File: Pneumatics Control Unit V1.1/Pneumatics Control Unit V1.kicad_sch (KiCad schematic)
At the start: 69 parts, among them J1 RX_PORT, J10 Conn_01x02_Male, J11 Conn_01x02_Male, J12 10118194-0001LF, J2 RX_PORT, J3 MICROMOD-2222, J4 Conn_01x02_Male, J5 Conn_01x02_Male, J6 Conn_01x02_Male, J7 Conn_01x02_Male, J8 Conn_01x02_Male, J9 Conn_01x02_Male, U1 ISL83490IBZ, U2 MIC2178-3.3YWM, U3 MC78M05CDTRKG

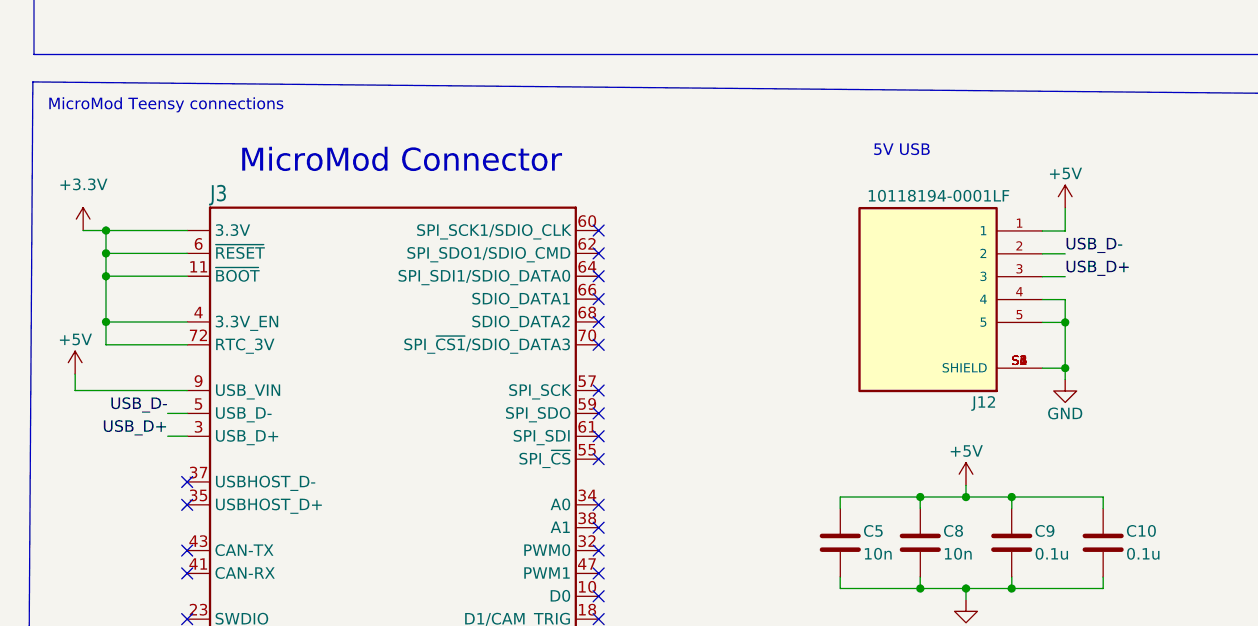
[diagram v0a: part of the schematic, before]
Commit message: Adding better m.2 connector
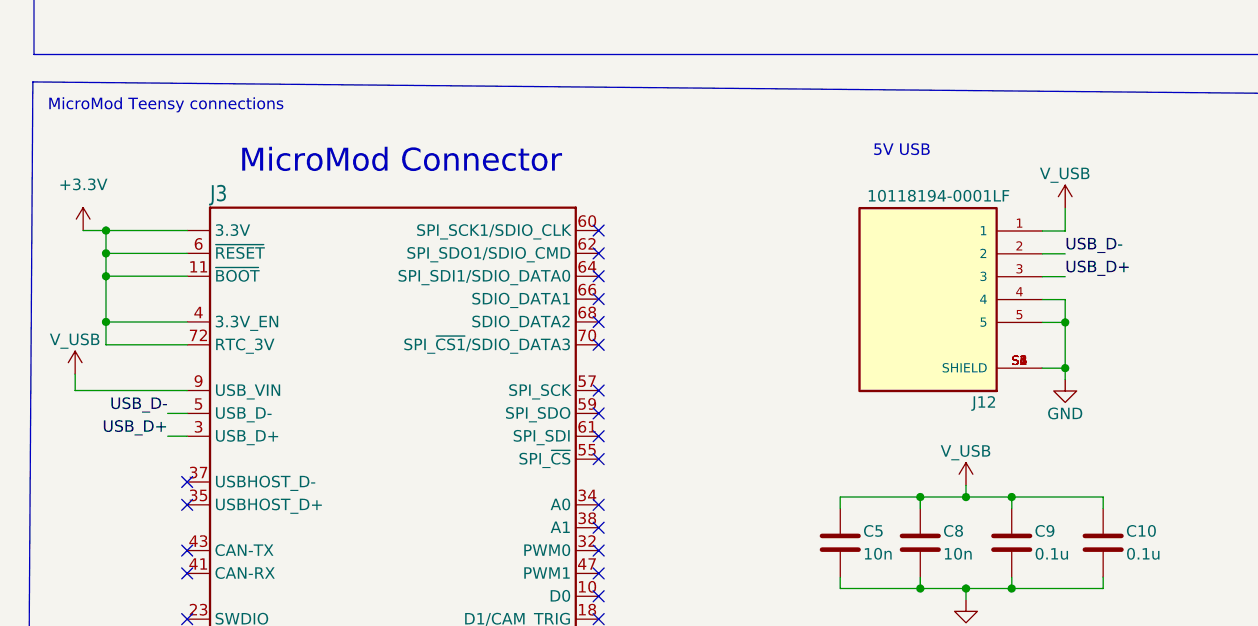
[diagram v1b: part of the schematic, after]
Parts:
- J3: footprint m2:MDT420M02001 -> mm-m:M.2-CONNECTOR-E
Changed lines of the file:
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@@
       (effects (font (size 1.27 1.27)) hide)
     )
-    (property "Value" "+5V" (id 1) (at 20.193 129.4892 0))
+    (property "Value" "V_USB" (id 1) (at 20.193 129.4892 0))
     (property "Footprint" "" (id 2) (at 20.193 133.2992 0)
       (effects (font (size 1.27 1.27)) hide)
@@
       (effects (font (size 1.778 1.5113)) (justify left bottom))
     )
-    (property "Footprint" "m2:MDT420M02001" (id 2) (at 55.499 168.148 0)
+    (property "Footprint" "mm-m:M.2-CONNECTOR-E" (id 2) (at 55.499 168.148 0)
       (effects (font (size 1.27 1.27)) hide)
     )
@@
       (effects (font (size 1.27 1.27)) hide)
     )
-    (property "Value" "+5V" (id 1) (at 130.2004 111.0488 0))
+    (property "Value" "V_USB" (id 1) (at 130.2004 111.0488 0))
     (property "Footprint" "" (id 2) (at 130.2004 114.8588 0)
       (effects (font (size 1.27 1.27)) hide)
@@
       (effects (font (size 1.27 1.27)) hide)
     )
-    (property "Value" "+5V" (id 1) (at 119.1768 141.8844 0))
+    (property "Value" "V_USB" (id 1) (at 119.1768 141.8844 0))
     (property "Footprint" "" (id 2) (at 119.1768 145.6944 0)
       (effects (font (size 1.27 1.27)) hide)
@@
   (symbol_instances
     (path "/40797b21-861a-42dd-8087-91d198f1026e"
-      (reference "#PWR01") (unit 1) (value "+5V") (footprint "")
+      (reference "#PWR01") (unit 1) (value "V_USB") (footprint "")
     )
     (path "/e7c716df-c012-4512-a2b1-2b5b2ce1bcbd"
@@
     )
     (path "/d7330338-c0d5-4a64-b93d-2554a72179c2"
-      (reference "#PWR03") (unit 1) (value "+5V") (footprint "")
+      (reference "#PWR03") (unit 1) (value "V_USB") (footprint "")
     )
     (path "/504d002d-27ba-46c5-b445-3a605faf93e7"
@@
     )
     (path "/a86e8a6a-4a69-44ee-b851-2e958dc4871a"
-      (reference "#PWR05") (unit 1) (value "+5V") (footprint "")
+      (reference "#PWR05") (unit 1) (value "V_USB") (footprint "")
     )
     (path "/4dfe37f2-1b83-4477-ab68-9396d2831d3d"
@@
     )
     (path "/9711fd24-5ce9-404b-9f31-8acd85b963f3"
-      (reference "J3") (unit 1) (value "MICROMOD-2222") (footprint "m2:MDT420M02001")
+      (reference "J3") (unit 1) (value "MICROMOD-2222") (footprint "mm-m:M.2-CONNECTOR-E")
     )
     (path "/920f195c-8d76-4e1c-95cf-b679803c48bf"

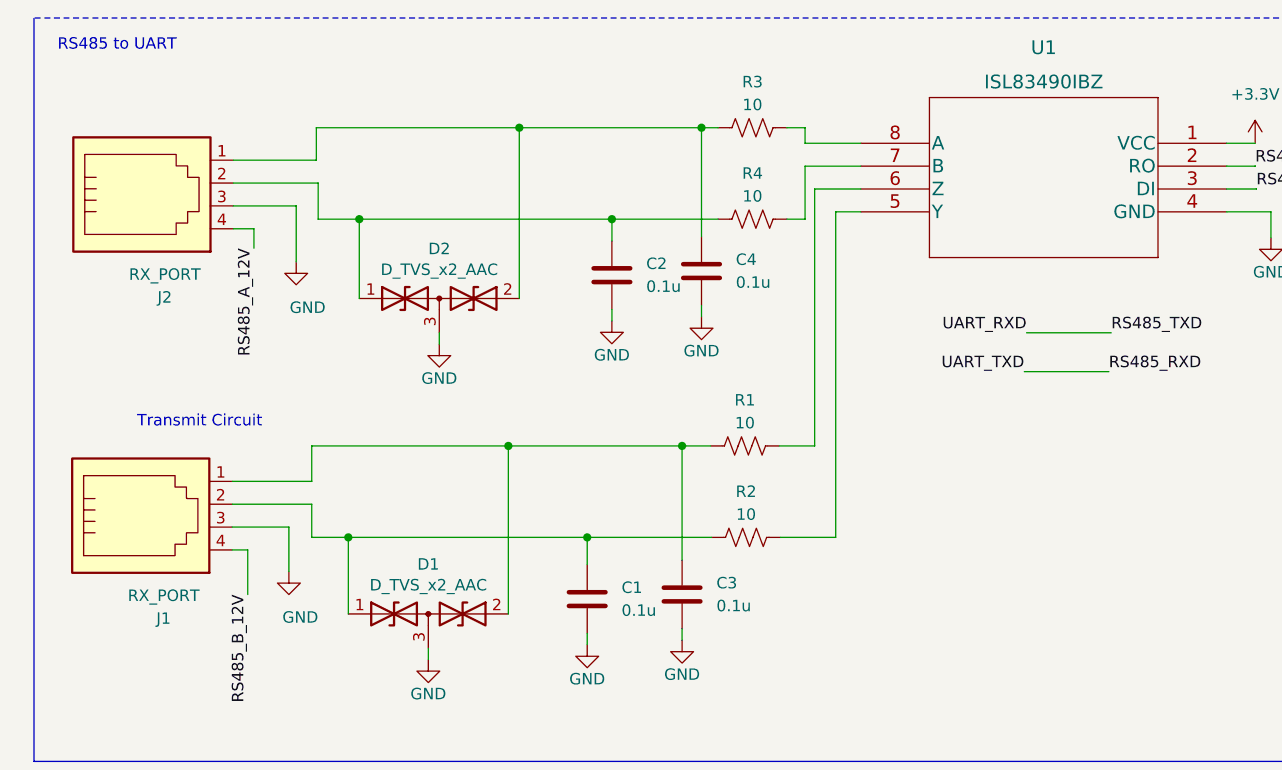
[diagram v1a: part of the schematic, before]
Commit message: Fixing the PCB silkscreen
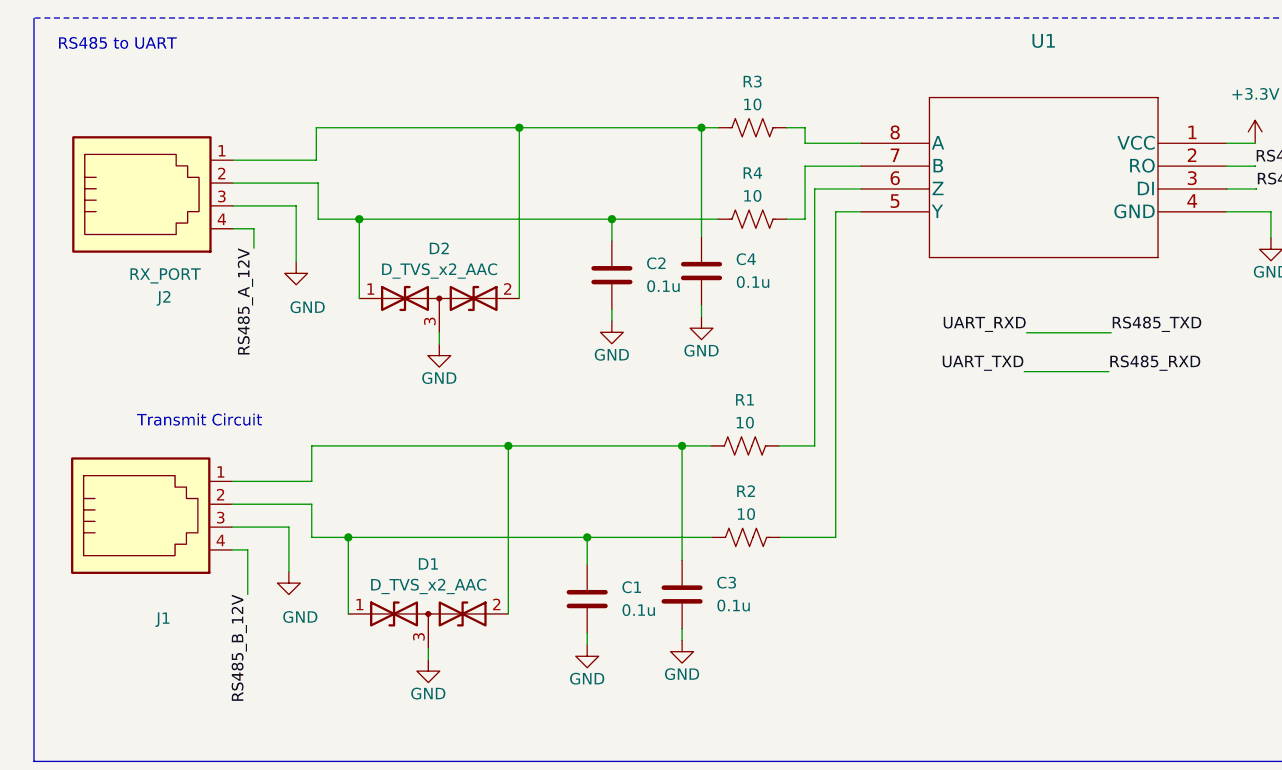
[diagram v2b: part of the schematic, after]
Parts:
- J1: value RX_PORT -> (none)
- U1: value ISL83490IBZ -> (none)
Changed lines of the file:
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@@
   (symbol (lib_id "2022-03-23_15-47-26:ISL83490IBZ") (at 148.1328 29.1084 0) (mirror y) (unit 1)
     (in_bom yes) (on_board yes) (fields_autoplaced)
-    (property "Reference" "U1" (id 0) (at 127.8128 18.4912 0)
-      (effects (font (size 1.524 1.524)))
-    )
-    (property "Value" "ISL83490IBZ" (id 1) (at 127.8128 22.3012 0)
+    (property "Reference" "U1" (id 0) (at 127.8128 17.78 0)
+      (effects (font (size 1.524 1.524)))
+    )
+    (property "Value" "" (id 1) (at 127.8128 21.59 0)
       (effects (font (size 1.524 1.524)))
     )
@@
     (in_bom yes) (on_board yes)
     (property "Reference" "J1" (id 0) (at 30.0228 81.915 0))
-    (property "Value" "RX_PORT" (id 1) (at 30.0228 79.375 0))
+    (property "Value" "" (id 1) (at 30.0228 79.375 0))
     (property "Footprint" "RS485:RS485" (id 2) (at 27.4828 70.485 90)
       (effects (font (size 1.27 1.27)) hide)
@@
     )
     (path "/2713445a-5e01-40d8-94c6-c4d9a94c1daa"
-      (reference "J1") (unit 1) (value "RX_PORT") (footprint "RS485:RS485")
+      (reference "J1") (unit 1) (value "TX_PORT") (footprint "RS485:RS485")
     )
     (path "/f46360b3-2778-4224-b87e-99e44d6e0b71"

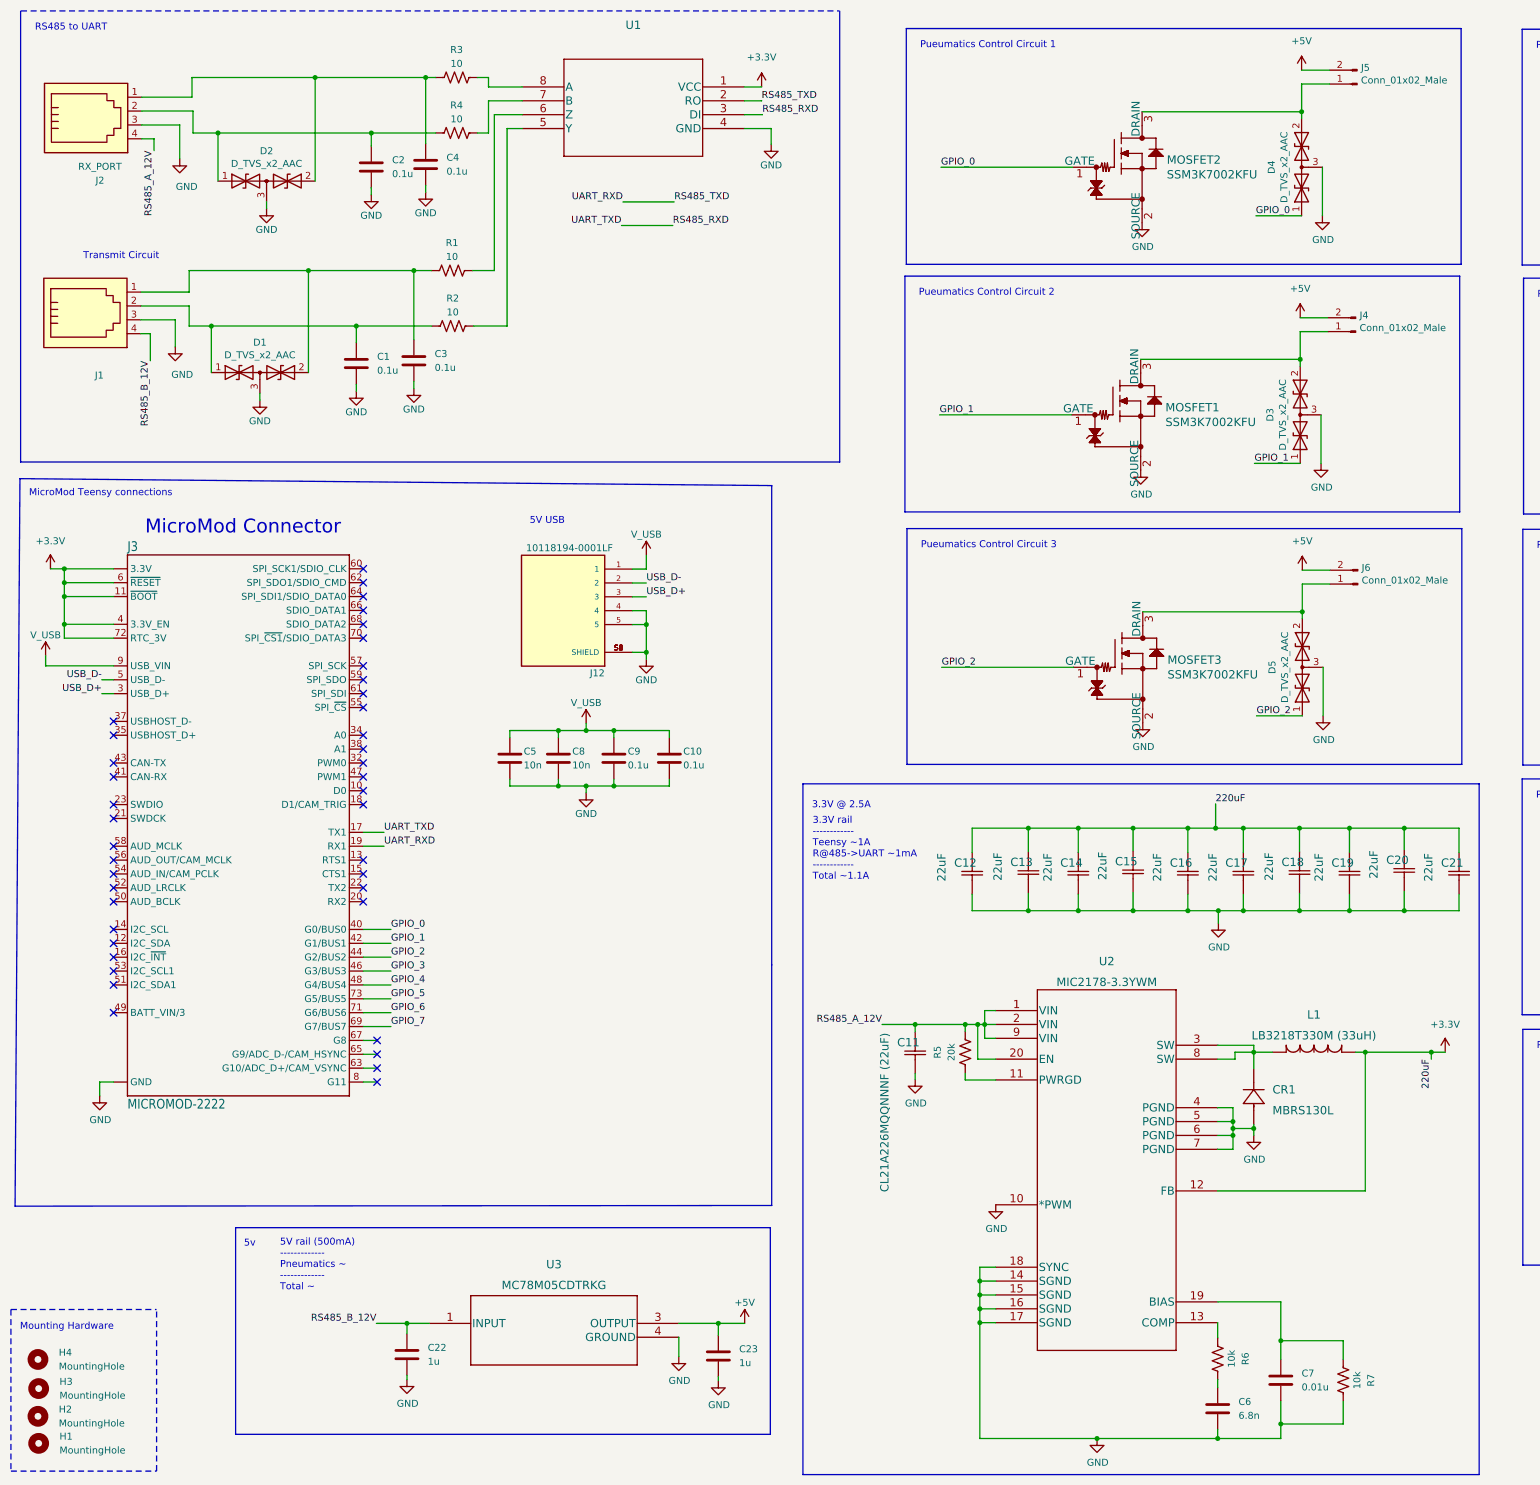
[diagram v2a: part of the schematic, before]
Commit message: Adding some caps to the switching and clearing errors
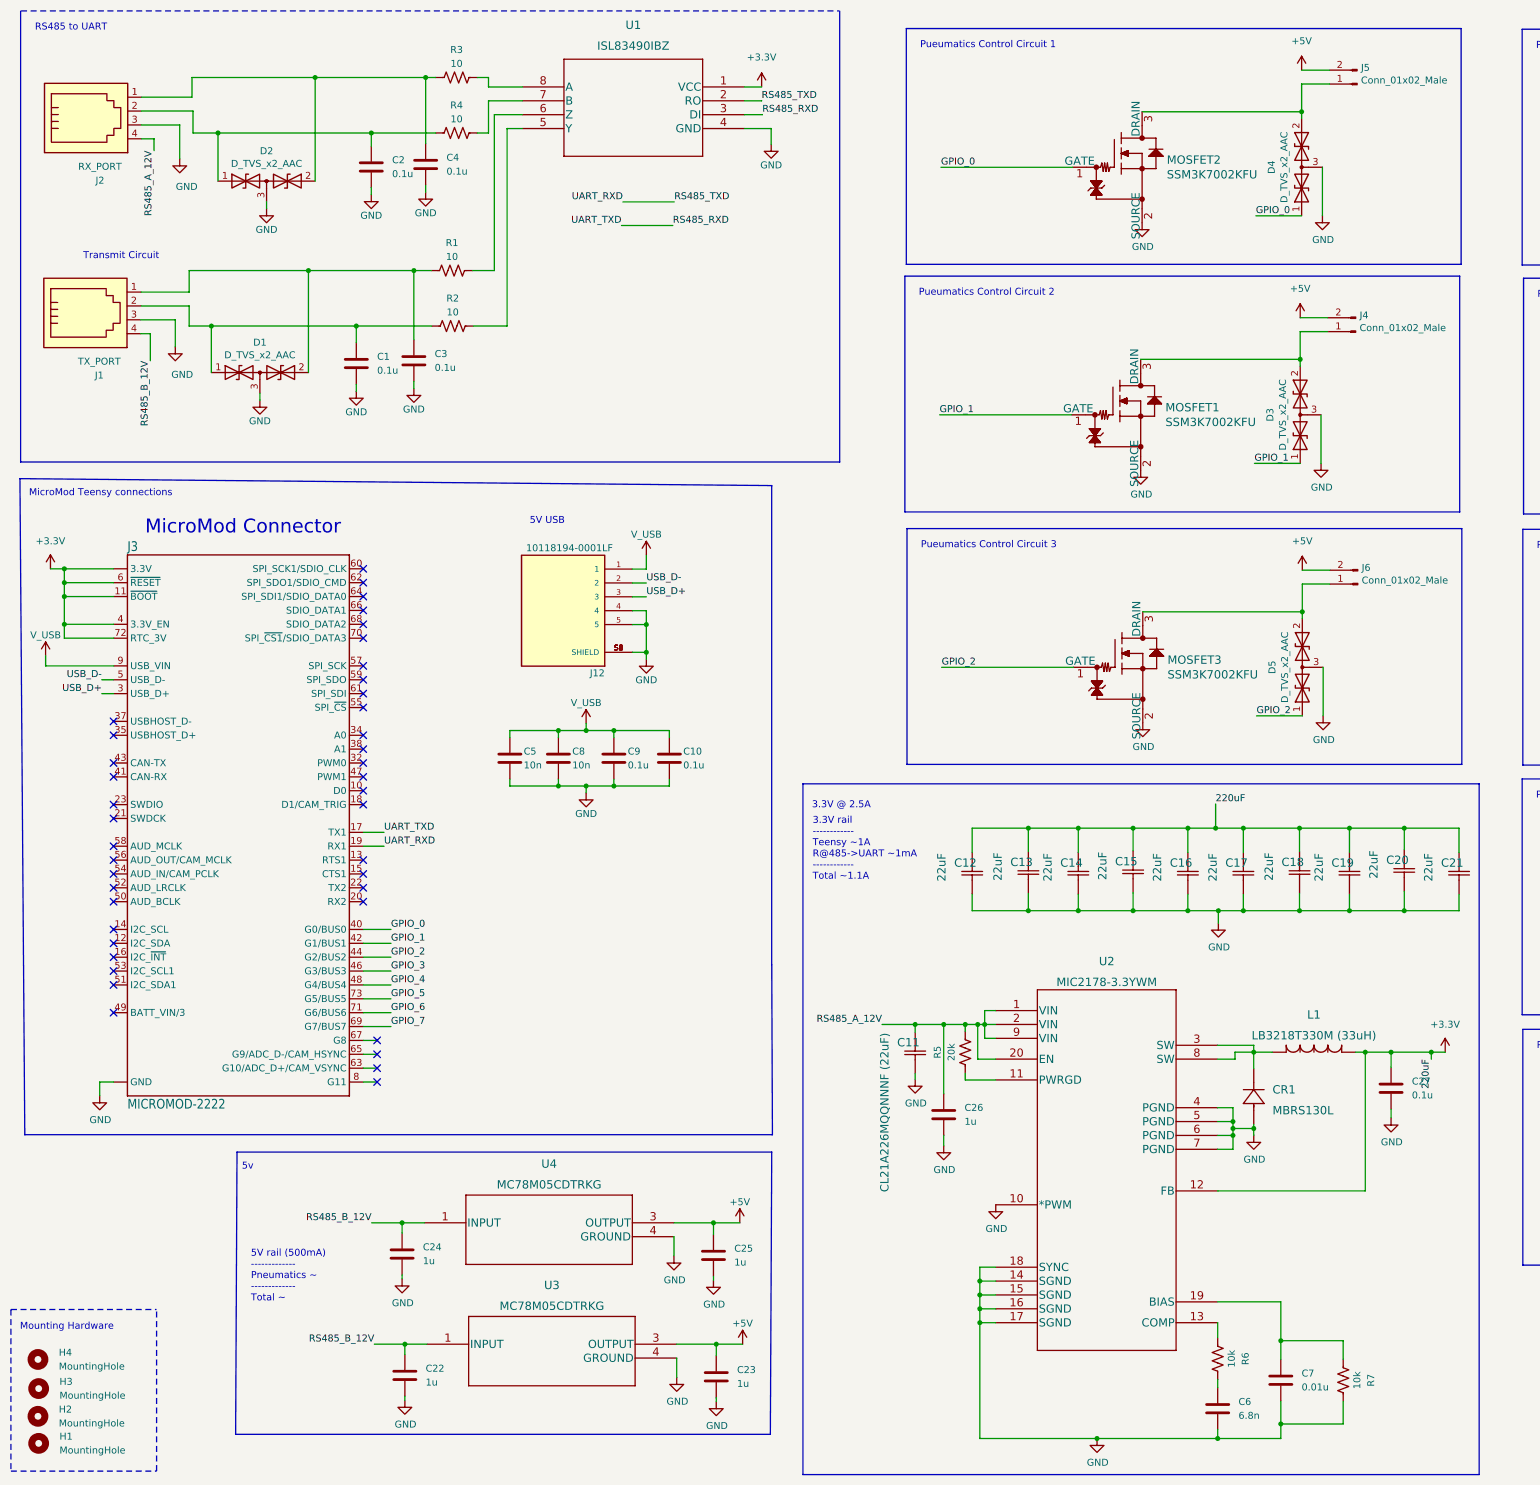
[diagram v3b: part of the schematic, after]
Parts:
- added C24, C25, C26: 1u, Capacitor_SMD:C_0805_2012Metric_Pad1.18x1.45mm_HandSolder, symbol Device:C
- added C27: 0.1u, Capacitor_SMD:C_0805_2012Metric_Pad1.18x1.45mm_HandSolder, symbol Device:C
- added U4: MC78M05CDTRKG, 12v5v:MC78M05CDTRKG, symbol 12V5V:MC78M05CDTRKG
- J1: value (none) -> TX_PORT
- U1: value (none) -> ISL83490IBZ
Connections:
- net 220uF: now also C27.1
- net GND: now also C24.2, C25.2, C26.2, C27.2, U4.4 (GROUND)
- net RS485_A_12V: now also C26.1
- net RS485_B_12V: now also C24.1, U4.1 (INPUT)
- new net: C25.1, U4.3 (OUTPUT)
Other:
- moved on the sheet: C22, C23, U3
